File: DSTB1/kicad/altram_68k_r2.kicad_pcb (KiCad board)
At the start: 2 copper layers, 28.2 x 82 mm, 38 parts, among them IC1 IS42S16320D-7TL, IC2 SN74CB3T3245PW, IC3 SN74CB3T3245PW, J1 Conn_01x06_Pin, U1 68000D, U2 68000D, U3 XC95144XL-TQ100, U4 AMS1117-3.3, X1 IQXO-70

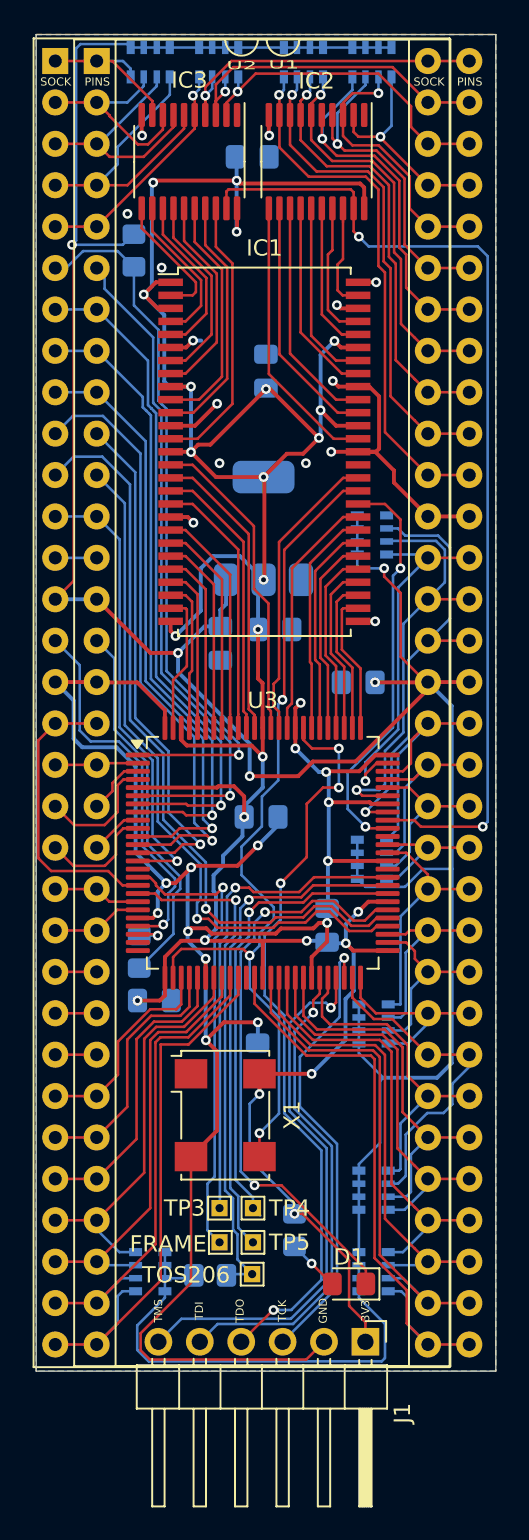
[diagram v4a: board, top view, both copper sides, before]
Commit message: Moved osc to the bottom layer and reworked traces for better ground plane for most of the board. Strapping added for two caps on the more isolated side.
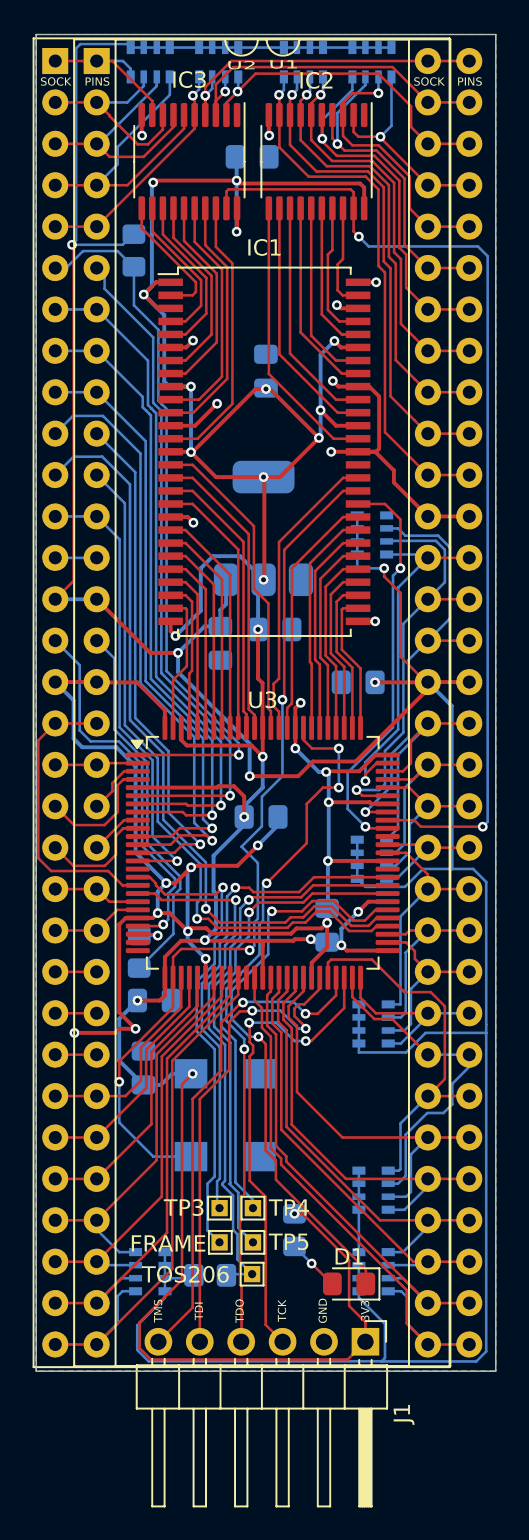
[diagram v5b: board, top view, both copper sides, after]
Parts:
- X1: moved to B.Cu
- moved C6 7.02 mm to (137.0, 117.4)
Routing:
- net GND: track 157.5 -> 128.4 mm, vias 28 -> 24
- net VCC: track 200.1 -> 221.4 mm
- net VCC3: track 192.2 -> 211.5 mm, vias 24 -> 23
- net /TMS: track 33.9 -> 30.6 mm, vias 1 -> 2
- net A11: track 20.7 -> 23.8 mm
- net /TDO: track 46.2 -> 43.7 mm
- net A5: track 36.5 -> 34.2 mm
- net A6: track 31.9 -> 29.7 mm
- net A7: track 28.6 -> 27.1 mm
- net A10: track 23.2 -> 24.6 mm
- net /TCK: track 28.2 -> 29.6 mm, vias 1 -> 2
- net A9: track 24.2 -> 25.3 mm
- net FC1: track 15.8 -> 14.7 mm
- net /TP3: track 30.0 -> 31.0 mm
- net FC0: track 18.4 -> 17.4 mm
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- removed copper zone on F.Cu, net GND
